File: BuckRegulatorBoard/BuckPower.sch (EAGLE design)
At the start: 5 parts, among them U1 LM2574N

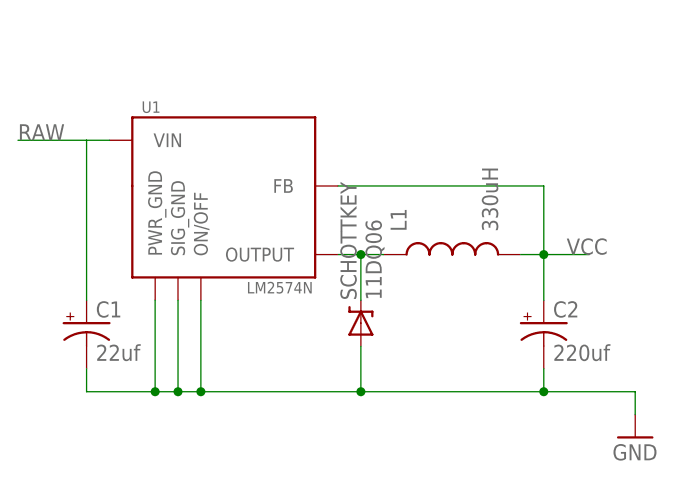
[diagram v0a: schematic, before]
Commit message: Tested versions of breakout boards
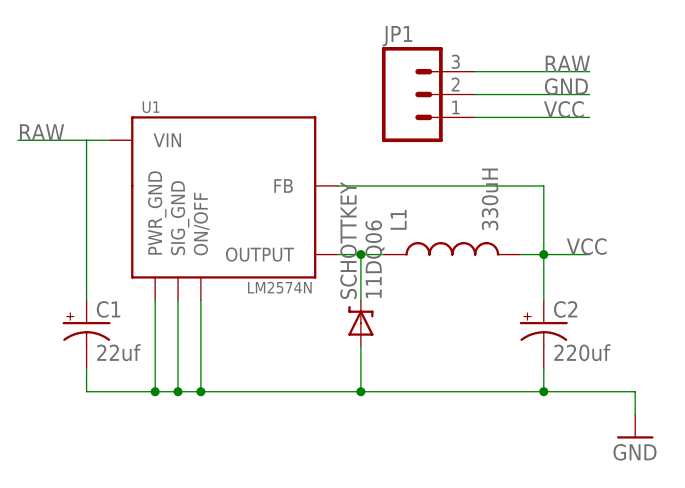
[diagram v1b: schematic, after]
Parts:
- added JP1: (no value), SparkFun:M031X03_NO_SILK
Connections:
- net GND: now also JP1.2
- net RAW: now also JP1.3
- net VCC: now also JP1.1
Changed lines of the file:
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@@
 <part name="L1" library="SparkFun" deviceset="INDUCTOR" device="H*" technology="1206" value="330uH"/>
 <part name="SCHOTTKEY" library="SparkFun" deviceset="DIODE-ZENER" device="PTH" value="11DQ06"/>
+<part name="JP1" library="SparkFun" deviceset="M03" device="1X03_NO_SILK"/>
 </parts>
 <sheets>
@@
 <instance part="L1" gate="G$1" x="68.58" y="40.64" rot="R90"/>
 <instance part="SCHOTTKEY" gate="G$1" x="58.42" y="33.02" rot="R90"/>
+<instance part="JP1" gate="G$1" x="63.5" y="58.42"/>
 </instances>
 <busses>
@@
 <wire x1="27.94" y1="53.34" x2="20.32" y2="53.34" width="0.1524" layer="91"/>
 <wire x1="27.94" y1="35.56" x2="27.94" y2="53.34" width="0.1524" layer="91"/>
+</segment>
+<segment>
+<pinref part="JP1" gate="G$1" pin="3"/>
+<wire x1="71.12" y1="60.96" x2="83.82" y2="60.96" width="0.1524" layer="91"/>
+<label x="78.74" y="60.96" size="1.778" layer="95"/>
 </segment>
 </net>
@@
 <wire x1="58.42" y1="25.4" x2="58.42" y2="30.48" width="0.1524" layer="91"/>
 </segment>
+<segment>
+<pinref part="JP1" gate="G$1" pin="2"/>
+<wire x1="71.12" y1="58.42" x2="83.82" y2="58.42" width="0.1524" layer="91"/>
+<label x="78.74" y="58.42" size="1.778" layer="95"/>
+</segment>
 </net>
 <net name="N$1" class="0">
@@
 <label x="81.28" y="40.64" size="1.778" layer="95"/>
 </segment>
+<segment>
+<pinref part="JP1" gate="G$1" pin="1"/>
+<wire x1="71.12" y1="55.88" x2="83.82" y2="55.88" width="0.1524" layer="91"/>
+<label x="78.74" y="55.88" size="1.778" layer="95"/>
+</segment>
 </net>
